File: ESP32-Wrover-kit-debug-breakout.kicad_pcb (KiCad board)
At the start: 2 copper layers, 85 x 83.1 mm, 4 parts, among them J1 Conn_02x14_Odd_Even, J2 Conn_02x04_Odd_Even, J3 Conn_02x07_Odd_Even, J4 Conn_02x05_Odd_Even

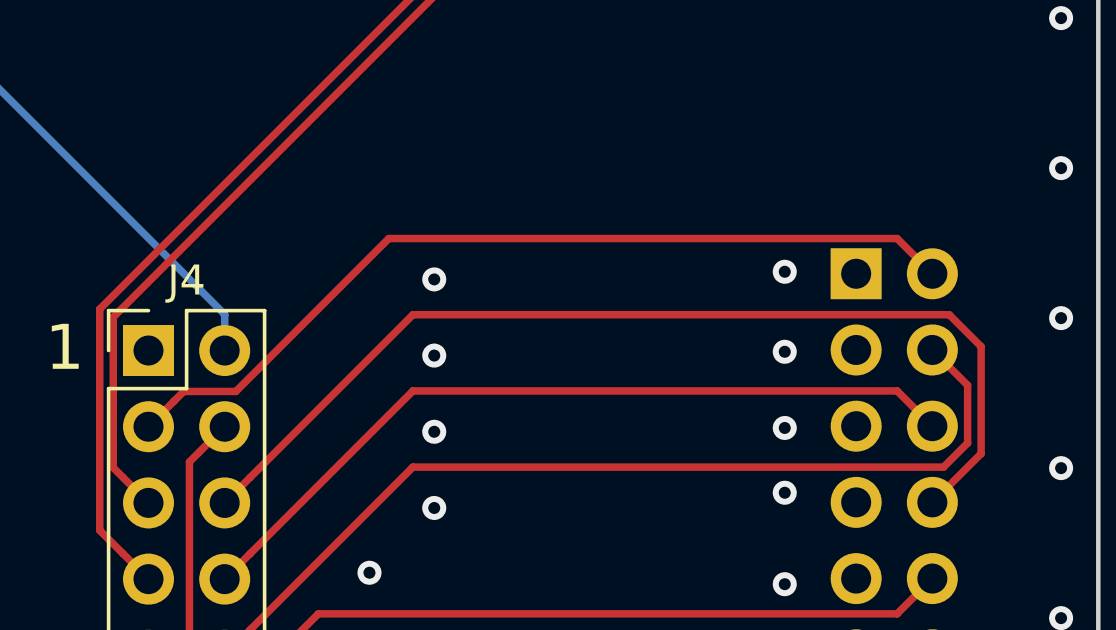
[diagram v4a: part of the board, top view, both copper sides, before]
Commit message: #2 It is acutally the Chip Enable signal we want, not nSRST since the enable signal is pulled low by the flasher.
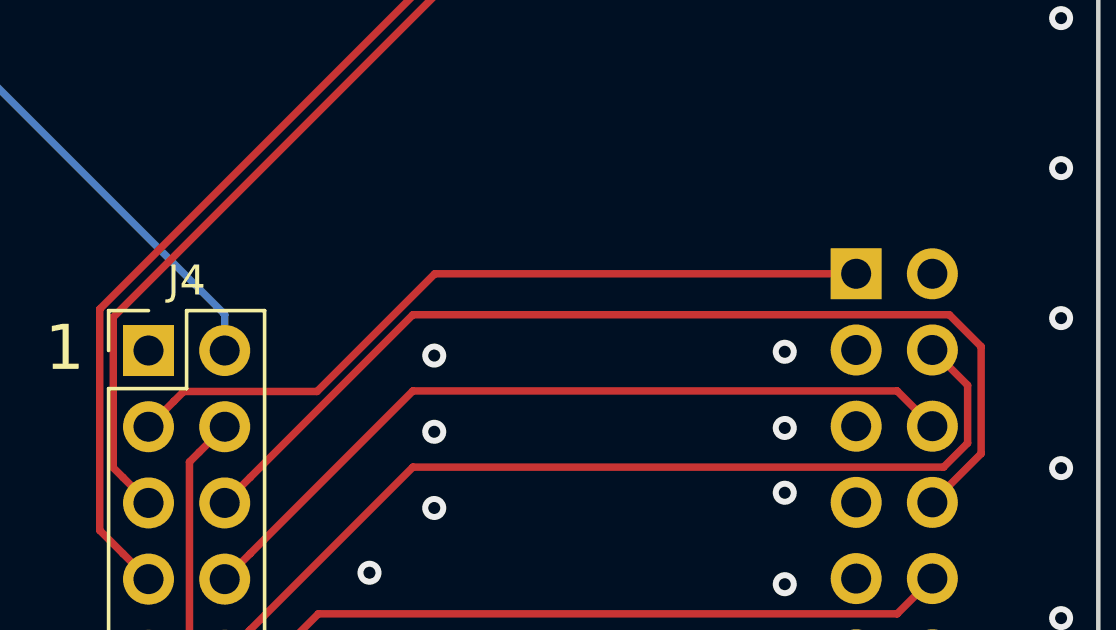
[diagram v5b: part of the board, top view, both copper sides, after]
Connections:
- J3 pad 1: Net-(J3-Pad1) -> /CH_Enable
- J3 pad 2: /CH_Enable -> Net-(J3-Pad2)
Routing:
- net /CH_Enable: track 29.2 -> 25.7 mm
- net GND: vias 76 -> 74
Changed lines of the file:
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@@
     (thickness 1.6)
     (drawings 15)
-    (tracks 125)
+    (tracks 122)
     (zones 0)
     (modules 4)
@@
   (net 49 "Net-(J3-Pad5)")
   (net 50 "Net-(J3-Pad3)")
-  (net 51 "Net-(J3-Pad1)")
+  (net 51 "Net-(J3-Pad2)")
   (net_class Default "This is the default net class."
     (clearance 0.2)
@@
     (add_net "Net-(J2-Pad6)")
     (add_net "Net-(J2-Pad8)")
-    (add_net "Net-(J3-Pad1)")
     (add_net "Net-(J3-Pad11)")
     (add_net "Net-(J3-Pad12)")
     (add_net "Net-(J3-Pad13)")
     (add_net "Net-(J3-Pad14)")
+    (add_net "Net-(J3-Pad2)")
     (add_net "Net-(J3-Pad3)")
     (add_net "Net-(J3-Pad5)")
@@
       (net 50 "Net-(J3-Pad3)"))
     (pad 2 thru_hole oval (at -2.54 0 180) (size 1.7 1.7) (drill 1) (layers *.Cu *.Mask)
+      (net 51 "Net-(J3-Pad2)"))
+    (pad 1 thru_hole rect (at 0 0 180) (size 1.7 1.7) (drill 1) (layers *.Cu *.Mask)
       (net 6 /CH_Enable))
-    (pad 1 thru_hole rect (at 0 0 180) (size 1.7 1.7) (drill 1) (layers *.Cu *.Mask)
-      (net 51 "Net-(J3-Pad1)"))
     (model ${KISYS3DMOD}/Connector_PinSocket_2.54mm.3dshapes/PinSocket_2x07_P2.54mm_Vertical.wrl
       (at (xyz 0 0 0))
@@
   (via (at 124.549 109.732) (size 0.8) (drill 0.4) (layers F.Cu B.Cu) (net 5))
   (via (at 124.549 107.192) (size 0.8) (drill 0.4) (layers F.Cu B.Cu) (net 5))
-  (via (at 124.549 104.525) (size 0.8) (drill 0.4) (layers F.Cu B.Cu) (net 5))
-  (via (at 112.865 104.779) (size 0.8) (drill 0.4) (layers F.Cu B.Cu) (net 5))
   (via (at 112.865 107.319) (size 0.8) (drill 0.4) (layers F.Cu B.Cu) (net 5))
   (segment (start 104.189999 108.840001) (end 103.34 109.69) (width 0.25) (layer F.Cu) (net 6))
   (segment (start 104.515001 108.514999) (end 104.189999 108.840001) (width 0.25) (layer F.Cu) (net 6))
-  (segment (start 106.254003 108.514999) (end 104.515001 108.514999) (width 0.25) (layer F.Cu) (net 6))
-  (segment (start 111.352003 103.416999) (end 106.254003 108.514999) (width 0.25) (layer F.Cu) (net 6))
-  (segment (start 128.293999 103.416999) (end 111.352003 103.416999) (width 0.25) (layer F.Cu) (net 6))
-  (segment (start 129.469 104.592) (end 128.293999 103.416999) (width 0.25) (layer F.Cu) (net 6))
+  (segment (start 108.958591 108.514999) (end 104.515001 108.514999) (width 0.25) (layer F.Cu) (net 6))
+  (segment (start 112.88159 104.592) (end 108.958591 108.514999) (width 0.25) (layer F.Cu) (net 6))
+  (segment (start 126.929 104.592) (end 112.88159 104.592) (width 0.25) (layer F.Cu) (net 6))
   (segment (start 57.199999 86.409999) (end 56.35 85.56) (width 0.25) (layer B.Cu) (net 7) (status 30))
   (segment (start 57.525001 86.735001) (end 57.199999 86.409999) (width 0.25) (layer B.Cu) (net 7) (status 20))

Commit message: Update PCB manufacturing files.
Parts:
- added REF**: OSHW-Logo2_9.8x8mm_SilkScreen, Symbol:OSHW-Logo2_9.8x8mm_SilkScreen, F.Cu at (90.7, 62.7)
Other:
- board text added: "ESP32 Wrover Kit breakout board | 2018 GitHub: PerMalmberg"
- board text removed: "ESP32 Wrover Kit breakout board | 2018 GitHub: PerMalmberg | IRC/freenode: Yoari"

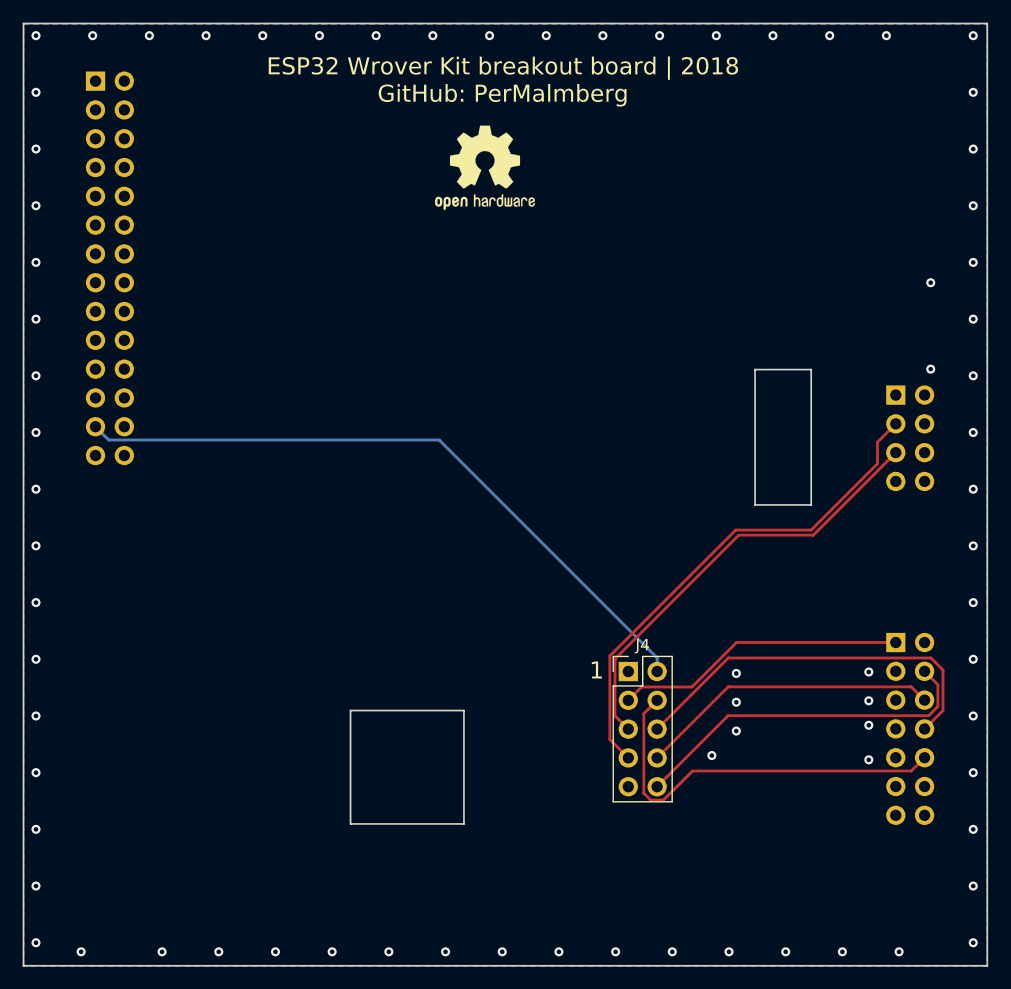
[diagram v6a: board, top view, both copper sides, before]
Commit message: Added soldering pads for IOs
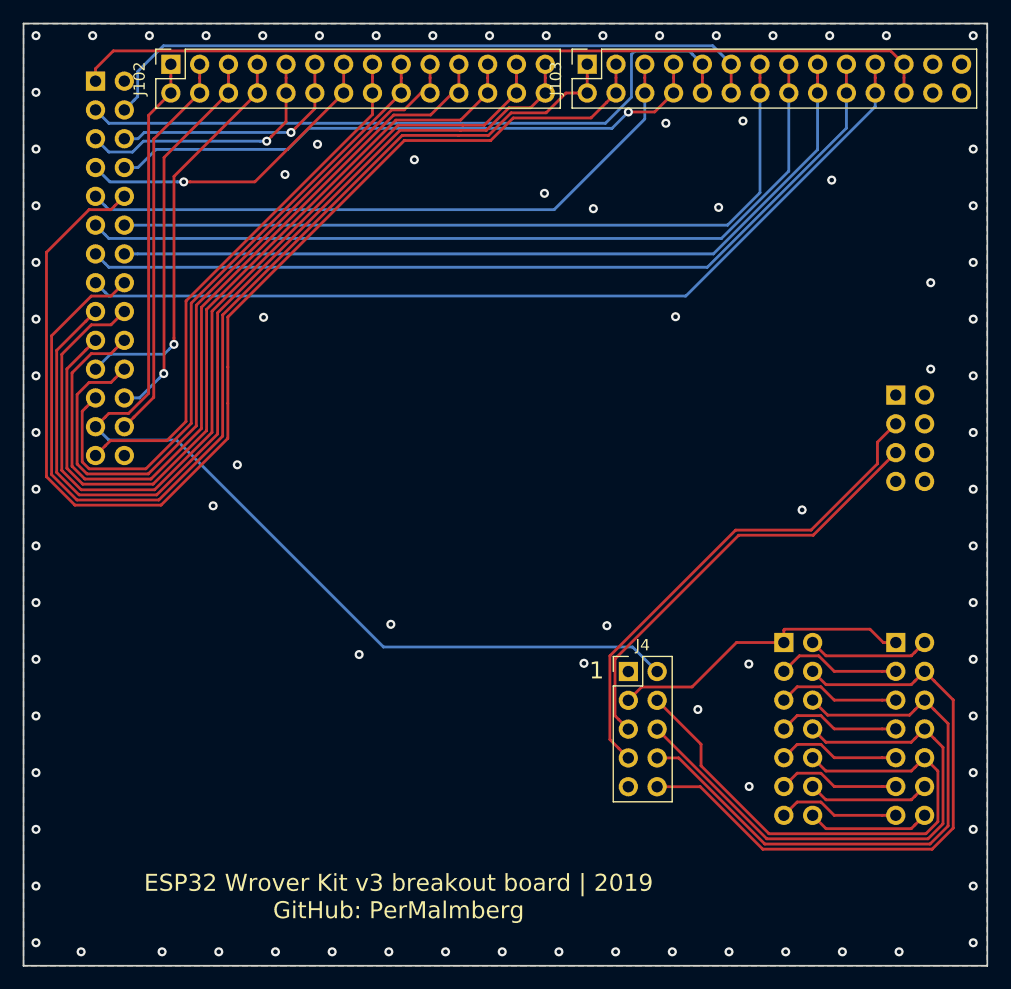
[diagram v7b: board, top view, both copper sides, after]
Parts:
- removed REF**: OSHW-Logo2_9.8x8mm_SilkScreen, Symbol:OSHW-Logo2_9.8x8mm_SilkScreen
- added J101: Conn_02x07_Odd_Even, Connector_PinSocket_2.54mm:PinSocket_2x07_P2.54mm_Vertical, B.Cu at (117.1, 104.6)
- added J102: Conn_02x14_Odd_Even, Connector_PinSocket_2.54mm:PinSocket_2x14_P2.54mm_Vertical, F.Cu at (63.0, 53.6)
- added J103: Conn_02x14_Odd_Even, Connector_PinSocket_2.54mm:PinSocket_2x14_P2.54mm_Vertical, F.Cu at (99.7, 53.6)
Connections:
- J1 pad 1: Net-(J1-Pad1) -> +3V3
- J1 pad 10: Net-(J1-Pad10) -> /GPIO_25
- J1 pad 11: Net-(J1-Pad11) -> /GPIO_35
- J1 pad 12: Net-(J1-Pad12) -> /GPIO_34
- J1 pad 13: Net-(J1-Pad13) -> /GPIO_39
- J1 pad 14: Net-(J1-Pad14) -> /GPIO_36
- J1 pad 15: Net-(J1-Pad15) -> /EN
- J1 pad 16: Net-(J1-Pad16) -> /GPIO_23
- J1 pad 17: Net-(J1-Pad17) -> /GPIO_22
- J1 pad 18: Net-(J1-Pad18) -> /GPIO_21
- J1 pad 19: Net-(J1-Pad19) -> /GPIO_19
- J1 pad 2: Net-(J1-Pad2) -> GND
- J1 pad 20: Net-(J1-Pad20) -> /GPIO_18
- J1 pad 21: Net-(J1-Pad21) -> /GPIO_5
- J1 pad 22: Net-(J1-Pad22) -> /GPIO_17
- J1 pad 23: Net-(J1-Pad23) -> /GPIO_16
- J1 pad 24: Net-(J1-Pad24) -> /GPIO_4
- J1 pad 26: Net-(J1-Pad26) -> /GPIO_2
- J1 pad 27: Net-(J1-Pad27) -> /GPIO_15
- J1 pad 3: Net-(J1-Pad3) -> /GPIO_32
- J1 pad 4: Net-(J1-Pad4) -> /GPIO_33
- J1 pad 5: Net-(J1-Pad5) -> /GPIO_12
- J1 pad 6: Net-(J1-Pad6) -> /GPIO_13
- J1 pad 7: Net-(J1-Pad7) -> /GPIO_14
- J1 pad 8: Net-(J1-Pad8) -> /GPIO_27
- J1 pad 9: Net-(J1-Pad9) -> /GPIO_26
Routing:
- net /GPIO_25: track 0.00 -> 103.8 mm
- net /GPIO_23: track 0.00 -> 92.4 mm
- net /GPIO_22: track 0.00 -> 83.0 mm
- net /GPIO_21: track 0.00 -> 81.4 mm
- net /EN: track 0.00 -> 79.9 mm
- net /GPIO_39: track 0.00 -> 77.4 mm
- net +3V3: track 0.00 -> 76.1 mm
- net /GPIO_35: track 0.00 -> 73.5 mm
- net /GPIO_19: track 0.00 -> 73.1 mm
- net /GPIO_36: track 0.00 -> 72.5 mm
- net /GPIO_18: track 0.00 -> 71.5 mm
- net /GPIO_34: track 0.00 -> 68.6 mm
- net /GPIO_17: track 0.00 -> 65.4 mm
- net /GPIO_32: track 0.00 -> 61.9 mm
- net /GPIO_33: track 0.00 -> 60.4 mm
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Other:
- outline, holes or cut-outs redrawn
- board text added: "ESP32 Wrover Kit v3 breakout board | 2019 GitHub: PerMalmberg"
- board text removed: "ESP32 Wrover Kit breakout board | 2018 GitHub: PerMalmberg"

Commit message: Added markers for GPIO.
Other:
- board text added: "+3.3V"
- board text added: "Boot option"
- board text added: "EN"
- board text added: "GND"
- board text added: "GPIO 12"
- board text added: "GPIO 13"
- board text added: "GPIO 14"
- board text added: "GPIO 15"
- board text added: "GPIO 16"
- board text added: "GPIO 17"
- board text added: "GPIO 18"
- board text added: "GPIO 19"
- board text added: "GPIO 2"
- board text added: "GPIO 21"
- board text added: "GPIO 22"
- board text added: "GPIO 23"
- board text added: "GPIO 25"
- board text added: "GPIO 26"
- board text added: "GPIO 27"
- board text added: "GPIO 32"
- board text added: "GPIO 33"
- board text added: "GPIO 34"
- board text added: "GPIO 35"
- board text added: "GPIO 36"
- board text added: "GPIO 39"
- board text added: "GPIO 4"
- board text added: "GPIO 5"
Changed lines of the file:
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@@
   (general
     (thickness 1.6)
-    (drawings 7)
+    (drawings 34)
     (tracks 462)
     (zones 0)
@@
     )
   )
-  (gr_text JLCJLCJLCJLC (at 120.56628 127.82188) (layer B.SilkS)
+  (gr_text GND (at 130.19796 60.476298 90) (layer F.SilkS)
+    (effects (font (size 1.5 1.5) (thickness 0.3)))
+  )
+  (gr_text +3.3V (at 127.7367 61.547726 90) (layer F.SilkS)
+    (effects (font (size 1.5 1.5) (thickness 0.3)))
+  )
+  (gr_text EN (at 125.00112 59.654869 90) (layer F.SilkS)
+    (effects (font (size 1.5 1.5) (thickness 0.3)))
+  )
+  (gr_text "GPIO 39" (at 122.49922 62.83344 90) (layer F.SilkS)
+    (effects (font (size 1.5 1.5) (thickness 0.3)))
+  )
+  (gr_text "GPIO 36" (at 119.96176 62.83344 90) (layer F.SilkS)
+    (effects (font (size 1.5 1.5) (thickness 0.3)))
+  )
+  (gr_text "GPIO 35" (at 117.48018 62.83344 90) (layer F.SilkS)
+    (effects (font (size 1.5 1.5) (thickness 0.3)))
+  )
+  (gr_text "GPIO 34" (at 114.9605 62.83344 90) (layer F.SilkS)
+    (effects (font (size 1.5 1.5) (thickness 0.3)))
+  )
+  (gr_text "GPIO 33" (at 112.51956 62.83344 90) (layer F.SilkS)
+    (effects (font (size 1.5 1.5) (thickness 0.3)))
+  )
+  (gr_text "GPIO 32" (at 110.01766 62.83344 90) (layer F.SilkS)
+    (effects (font (size 1.5 1.5) (thickness 0.3)))
+  )
+  (gr_text "GPIO 27" (at 107.28208 62.83344 90) (layer F.SilkS)
+    (effects (font (size 1.5 1.5) (thickness 0.3)))
+  )
+  (gr_text "GPIO 26" (at 104.80304 62.83344 90) (layer F.SilkS)
+    (effects (font (size 1.5 1.5) (thickness 0.3)))
+  )
+  (gr_text "GPIO 25" (at 102.20462 62.83344 90) (layer F.SilkS)
+    (effects (font (size 1.5 1.5) (thickness 0.3)))
+  )
+  (gr_text "GPIO 23" (at 99.66462 62.83344 90) (layer F.SilkS)
+    (effects (font (size 1.5 1.5) (thickness 0.3)))
+  )
+  (gr_text "GPIO 22" (at 96.04258 62.83344 90) (layer F.SilkS)
+    (effects (font (size 1.5 1.5) (thickness 0.3)))
+  )
+  (gr_text "GPIO 21" (at 93.44162 62.83344 90) (layer F.SilkS)
+    (effects (font (size 1.5 1.5) (thickness 0.3)))
+  )
+  (gr_text "GPIO 19" (at 90.90416 62.83344 90) (layer F.SilkS)
+    (effects (font (size 1.5 1.5) (thickness 0.3)))
+  )
+  (gr_text "GPIO 18" (at 88.40226 62.83344 90) (layer F.SilkS)
+    (effects (font (size 1.5 1.5) (thickness 0.3)))
+  )
+  (gr_text "GPIO 17" (at 85.96132 62.83344 90) (layer F.SilkS)
+    (effects (font (size 1.5 1.5) (thickness 0.3)))
+  )
+  (gr_text "GPIO 16" (at 83.3248 62.83344 90) (layer F.SilkS)
+    (effects (font (size 1.5 1.5) (thickness 0.3)))
+  )
+  (gr_text "GPIO 15" (at 80.64764 62.83344 90) (layer F.SilkS)
+    (effects (font (size 1.5 1.5) (thickness 0.3)))
+  )
+  (gr_text "GPIO 14" (at 78.28544 62.83344 90) (layer F.SilkS)
+    (effects (font (size 1.5 1.5) (thickness 0.3)))
+  )
+  (gr_text "GPIO 13" (at 75.72512 62.83344 90) (layer F.SilkS)
+    (effects (font (size 1.5 1.5) (thickness 0.3)))
+  )
+  (gr_text "GPIO 12" (at 73.18512 62.83344 90) (layer F.SilkS)
+    (effects (font (size 1.5 1.5) (thickness 0.3)))
+  )
+  (gr_text "GPIO 5" (at 70.60702 62.119155 90) (layer F.SilkS)
+    (effects (font (size 1.5 1.5) (thickness 0.3)))
+  )
+  (gr_text "GPIO 4" (at 68.0086 62.119155 90) (layer F.SilkS)
+    (effects (font (size 1.5 1.5) (thickness 0.3)))
+  )
+  (gr_text "GPIO 2" (at 65.41018 62.119155 90) (layer F.SilkS)
+    (effects (font (size 1.5 1.5) (thickness 0.3)))
+  )
+  (gr_text "Boot option" (at 62.8905 64.797726 90) (layer F.SilkS)
+    (effects (font (size 1.5 1.5) (thickness 0.3)))
+  )
+  (gr_text JLCJLCJLCJLC (at 123.38314 112.78 90) (layer B.SilkS)
     (effects (font (size 1 1) (thickness 0.25)) (justify mirror))
   )
